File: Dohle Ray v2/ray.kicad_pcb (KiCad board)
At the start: 2 copper layers, 46.9 x 67.5 mm, 34 parts, among them Q1 J201, SW1 Footswitch, U1 TL082

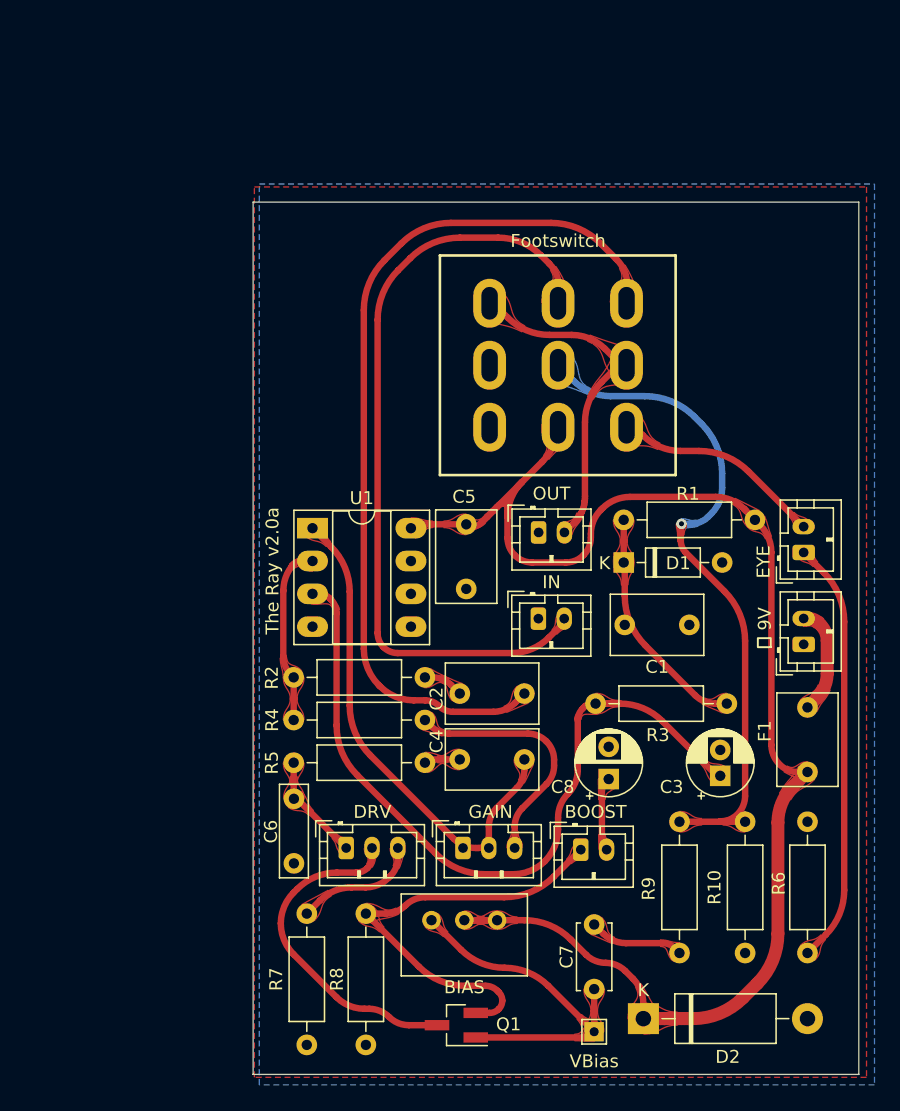
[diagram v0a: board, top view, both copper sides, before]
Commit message: Update the ray footswitch footprint
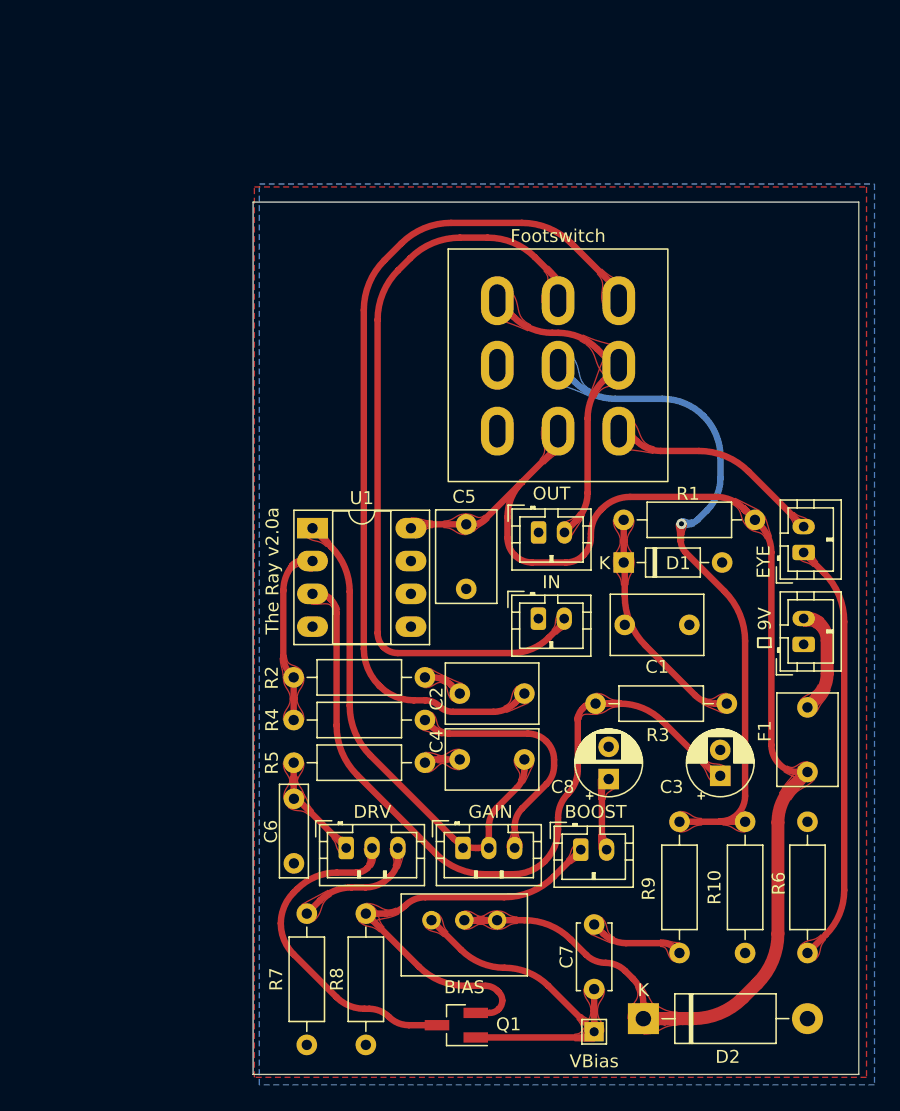
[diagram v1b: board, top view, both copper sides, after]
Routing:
- net +9V: track 113.0 -> 109.2 mm
- net FXIn: track 69.0 -> 67.6 mm
- net Net-(OUT1-Pad2): track 26.0 -> 25.2 mm

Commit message: String Maschine - finish voice board
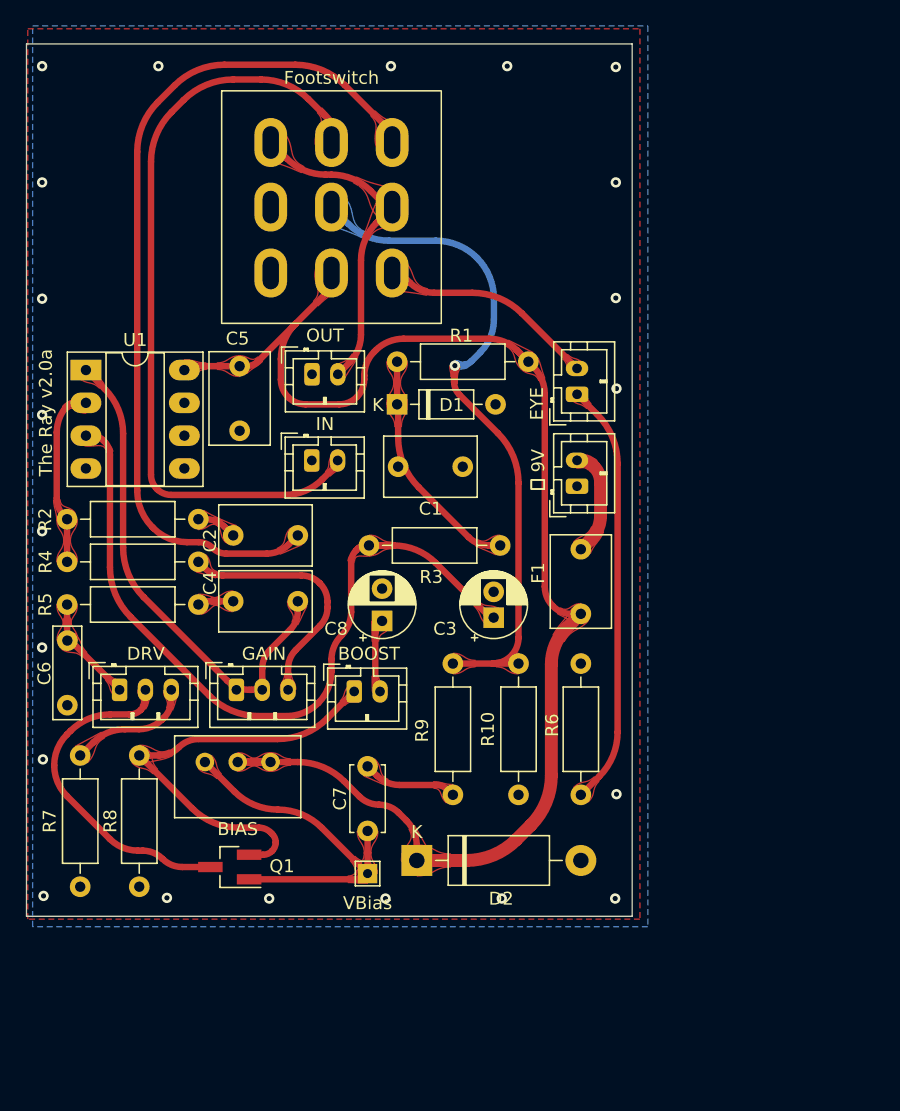
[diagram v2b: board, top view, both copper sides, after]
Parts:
- moved C1 21.4 mm to (131.6, 67.0)
- moved BOOST1 21.4 mm to (123.2, 84.4)
- moved R7 21.4 mm to (101.9, 99.5)
- moved R9 21.4 mm to (130.8, 82.2)
- moved R1 21.4 mm to (126.5, 58.9)
- moved SW1 21.4 mm to (122.1, 46.9)
- moved U1 21.4 mm to (102.4, 59.5)
- moved C2 21.4 mm to (118.8, 72.3)
- moved C4 21.4 mm to (118.8, 77.4)
- moved C5 21.4 mm to (114.3, 64.2)
- moved C6 21.4 mm to (101.0, 80.5)
- moved C7 21.4 mm to (124.2, 95.2)
- moved D1 21.4 mm to (126.5, 62.2)
- moved DRV1 21.4 mm to (105.0, 84.3)
- moved OUT1 21.4 mm to (119.9, 59.9)
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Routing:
- net GND: vias 0 -> 12
- net (no net): vias 0 -> 9
